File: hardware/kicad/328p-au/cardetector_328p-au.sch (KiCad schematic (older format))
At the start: 64 parts, among them IC1 ATMEGA328-A, K1 RELAY_1RT, P1 CONN_01X03, P2 ISP, P3 RELAY OUT, P4 TTL OUT, P5 I2C, Q1 BSS138, Q2 BC817-40, SW1 TACTILE_SW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

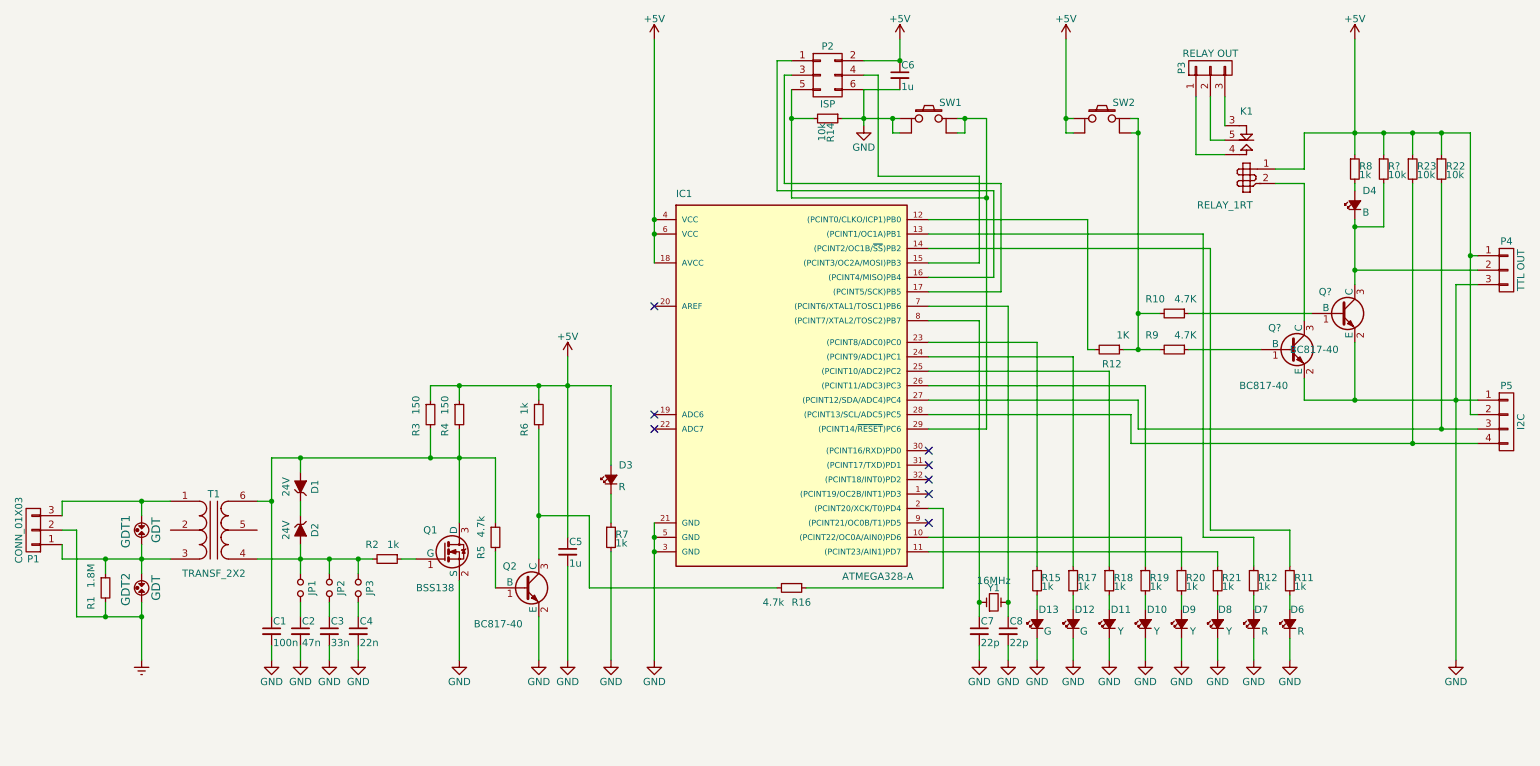
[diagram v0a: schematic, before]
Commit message: hardware/kicad/328p-au: separated output sheet
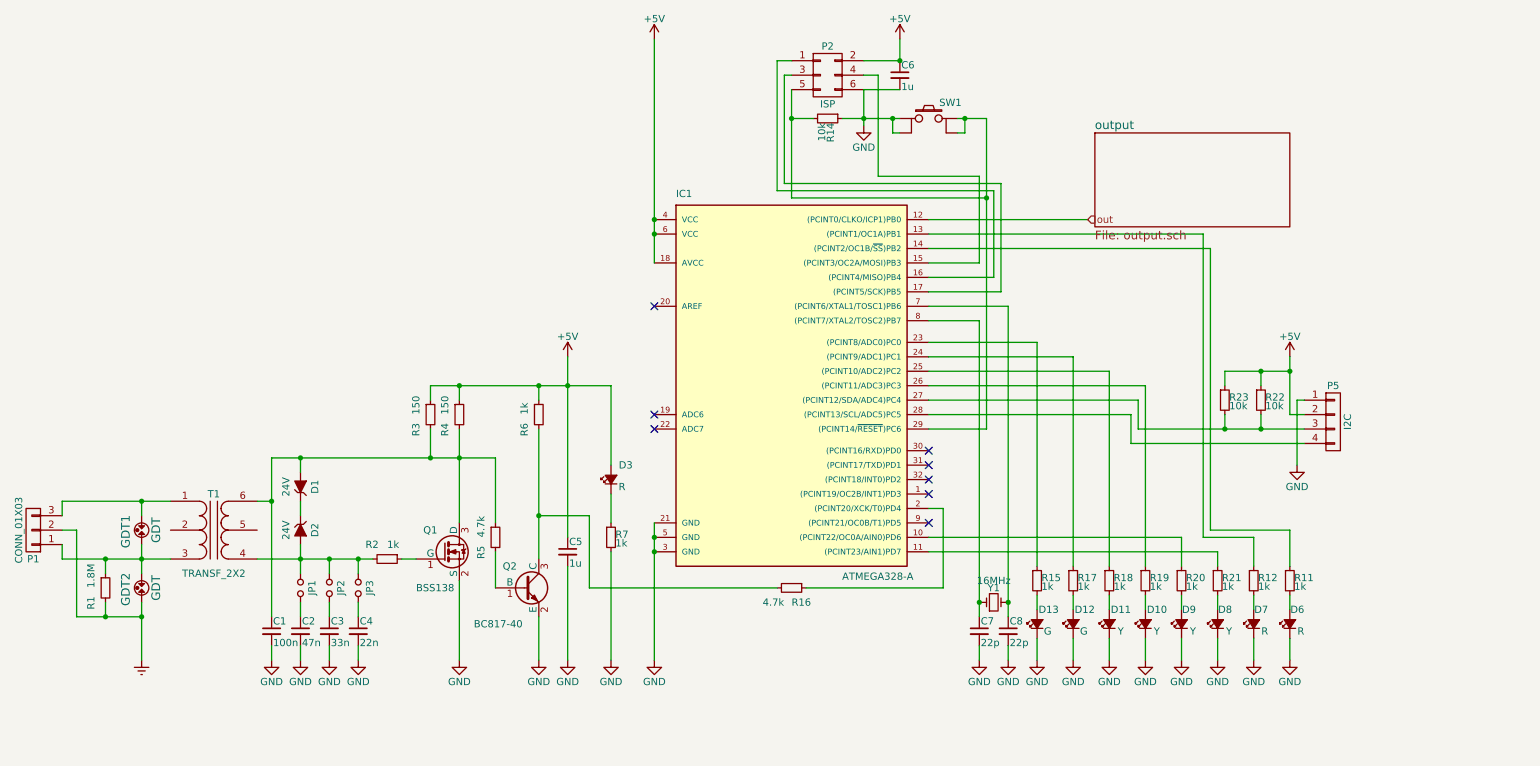
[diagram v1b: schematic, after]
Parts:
- removed D4: B, symbol Led_Small
- removed K1: RELAY_1RT, relays:SRD-SL-C, symbol RELAY_1RT
- removed P3: RELAY OUT, symbol CONN_01X03
- removed P4: TTL OUT, symbol CONN_01X03
- removed Q? (x2): BC817-40, SOT-23, symbol BC817-40
- removed R10, R9: 4.7K, symbol R_Small
- removed R12: 1K, symbol R_Small
- removed R8: 1k, symbol R_Small
- removed R?: 10k, symbol R_Small
- removed SW2: TACTILE_SW, symbol TACTILE_SW
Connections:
- net out: now reaches IC1.12 ((PCINT0/CLKO/ICP1)PB0)
- net at IC1.27 ((PCINT12/SDA/ADC4)PC4), P5.3 (P3), R22.2: now also R23.2
- net at IC1.28 ((PCINT13/SCL/ADC5)PC5), P5.4 (P4): no longer R23.2
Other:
- moved on the sheet: P5, R22, R23

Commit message: hardware/kicad/328p-au: separated collpits page, footprints assigned and imported to PCB
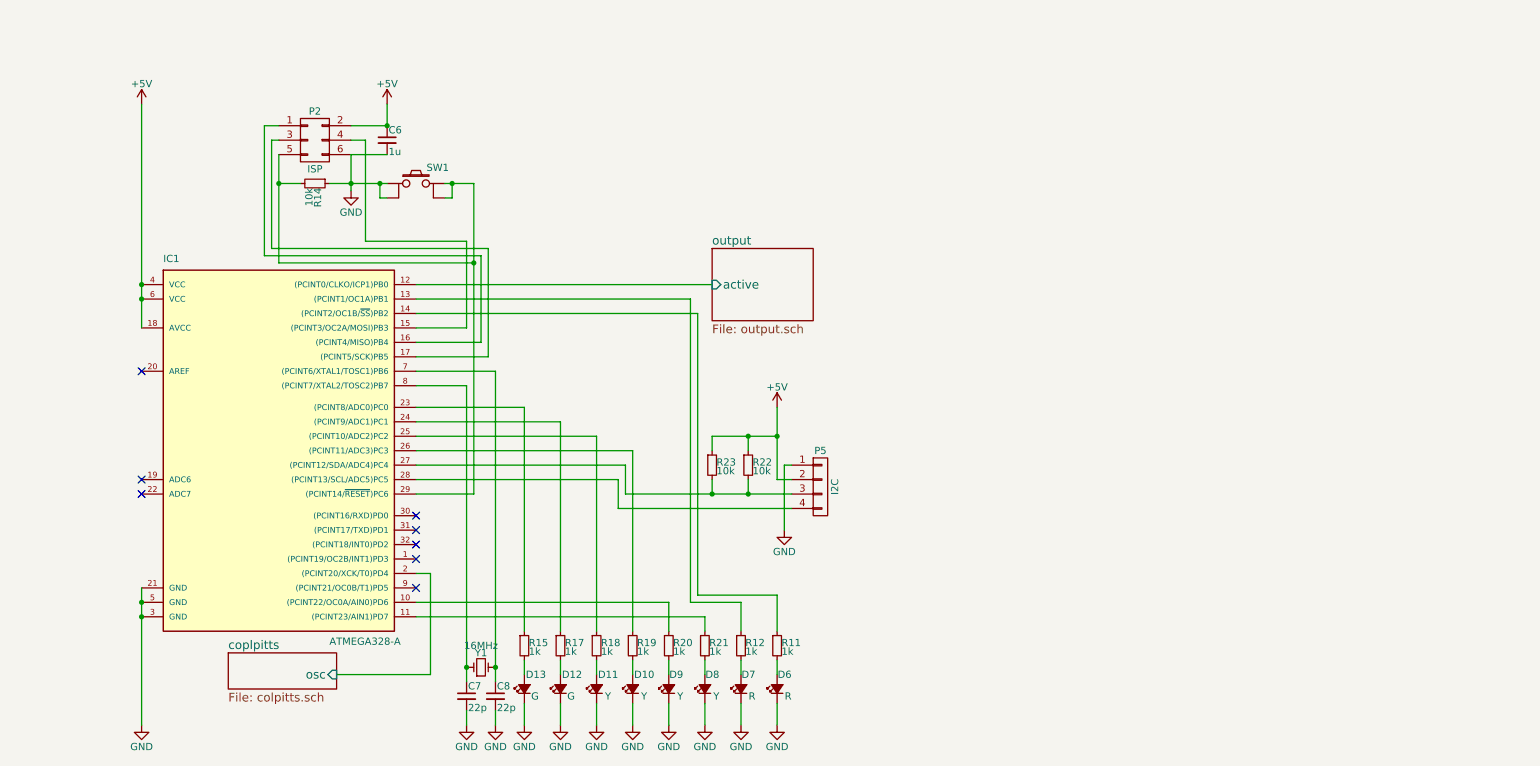
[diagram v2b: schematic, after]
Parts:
- removed C1: 100n, symbol C_Small
- removed C2: 47n, symbol C_Small
- removed C3: 33n, symbol C_Small
- removed C4: 22n, symbol C_Small
- removed C5: 1u, symbol C_Small
- removed D1, D2: 24V, symbol ZENERsmall
- removed D3: R, symbol Led_Small
- removed GDT1, GDT2: GDT, symbol GDT
- removed JP1, JP2, JP3: Jumper_NO_Small, symbol Jumper_NO_Small
- removed P1: CONN_01X03, symbol CONN_01X03
- removed Q1: BSS138, SOT-23, symbol BSS138
- removed Q2: BC817-40, SOT-23, symbol BC817-40
- removed R1: 1.8M, symbol R_Small
- removed R16, R5: 4.7k, symbol R_Small
- removed R2, R6, R7: 1k, symbol R_Small
- removed R3, R4: 150, symbol R_Small
- removed T1: TRANSF_2X2, symbol TRANSF_2X2
- C6, C7, C8: footprint (none) -> Capacitors_SMD:C_0603_HandSoldering
- D10, D11, D12, D13, D6, D7, D8, D9: footprint (none) -> gate433:SOD80C
- P2: footprint (none) -> Socket_Strips:Socket_Strip_Straight_2x03
- P5: footprint (none) -> Pin_Headers:Pin_Header_Straight_1x04
- R11, R12, R14, R15, R17, R18, R19, R20, R21, R22, R23: footprint (none) -> Resistors_SMD:R_0603_HandSoldering
- SW1: footprint (none) -> Buttons_Switches_ThroughHole:SW_TH_Tactile_Omron_B3F-10xx
- Y1: footprint (none) -> Crystals:Crystal_HC49-U_Vertical
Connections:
- net coplpitts/osc: now reaches IC1.2 ((PCINT20/XCK/T0)PD4)
- net out renamed output/active
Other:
- moved on the sheet: C6, C7, C8, D10, D11, D12, D13, D6, D7, D8, D9, IC1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

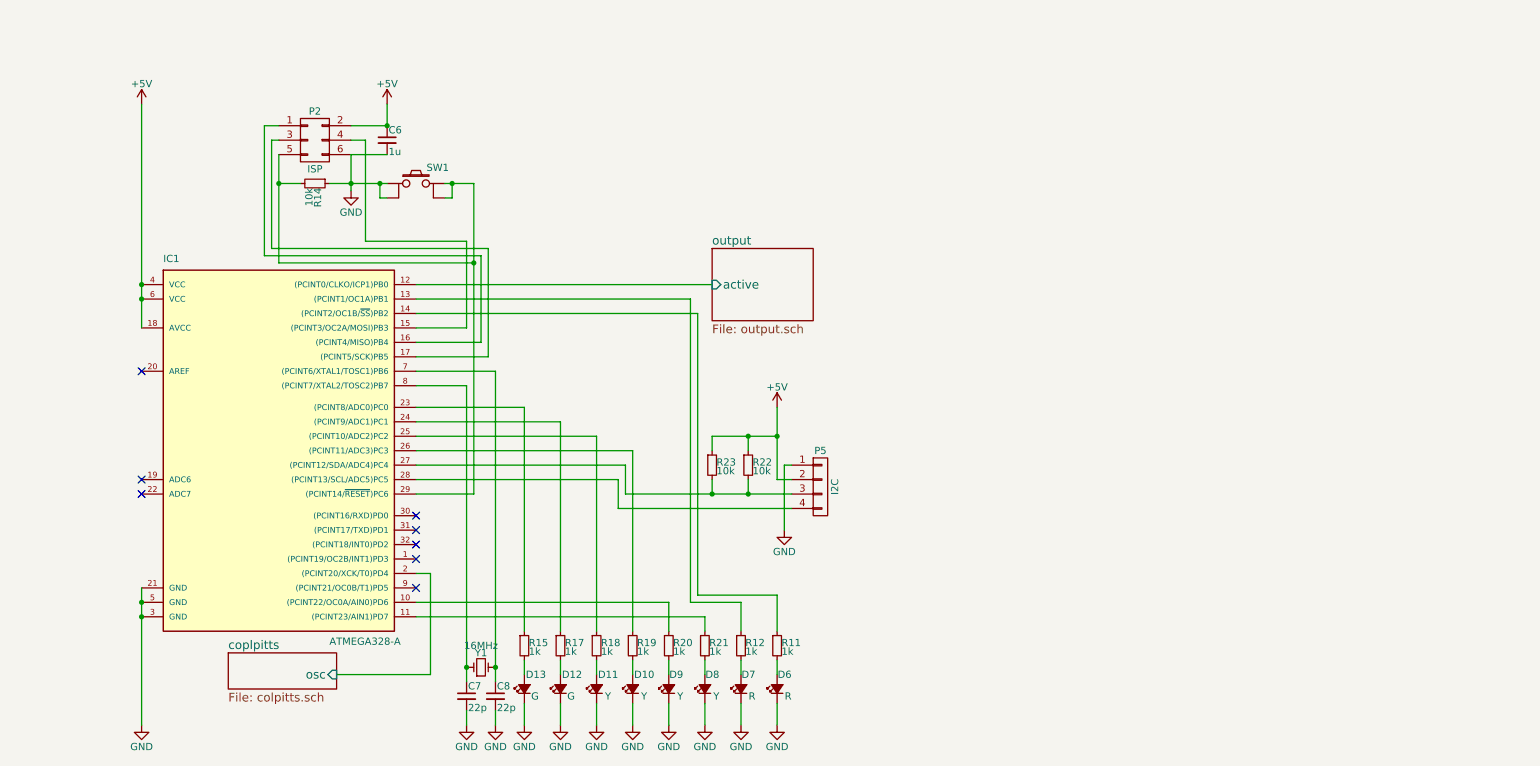
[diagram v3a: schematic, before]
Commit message: hardware/kicad: added serial connector && 3 push buttons
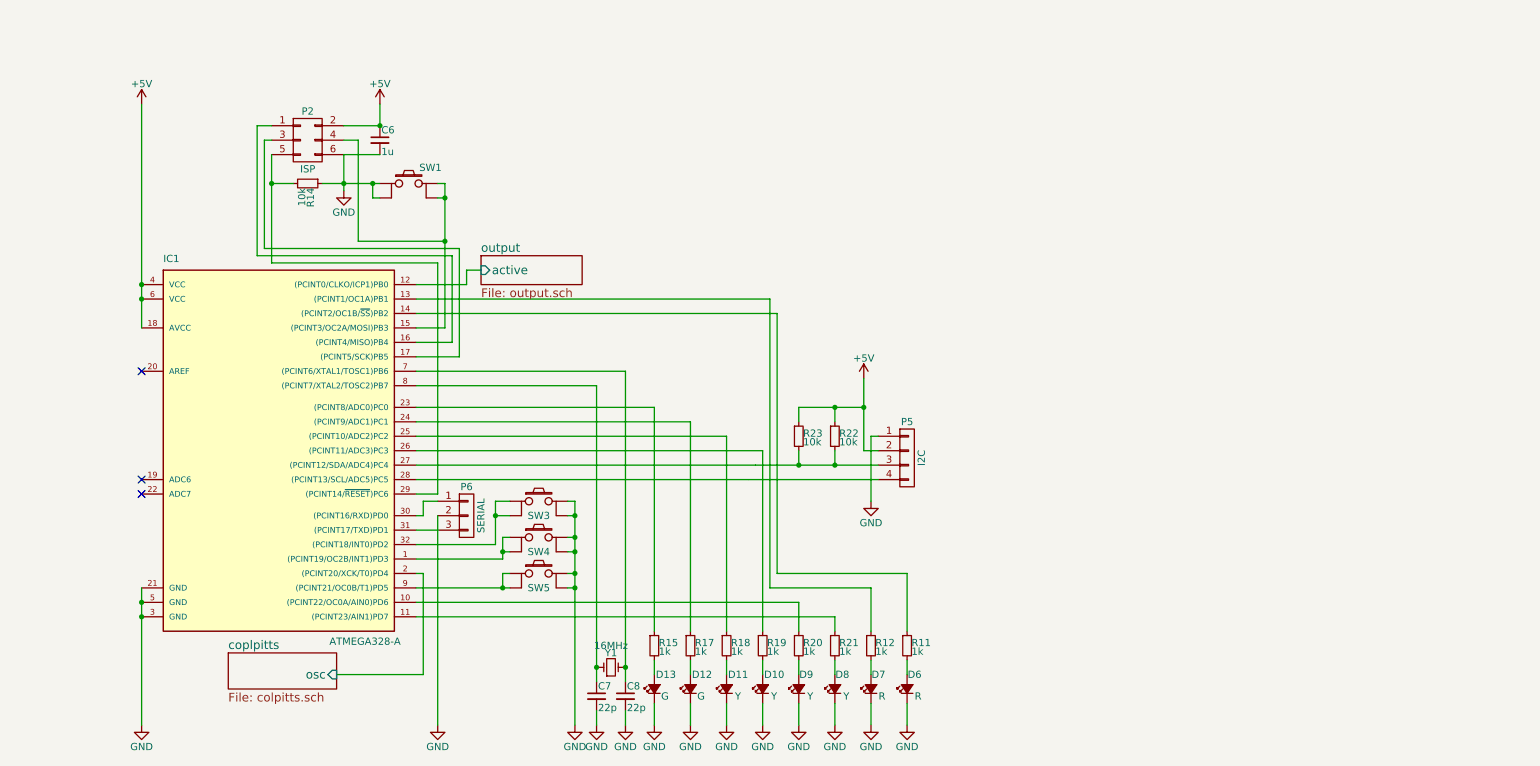
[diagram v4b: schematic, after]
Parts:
- added P6: SERIAL, Pin_Headers:Pin_Header_Straight_1x03, symbol CONN_01X03
- added SW3, SW4, SW5: TACTILE_SW, Buttons_Switches_ThroughHole:SW_TH_Tactile_Omron_B3F-10xx, symbol TACTILE_SW
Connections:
- net GND: now also P6.2 (P2), SW3.3, SW3.4, SW4.3, SW4.4, SW5.3, SW5.4
- net at IC1.15 ((PCINT3/OC2A/MOSI)PB3), P2.4 (P4): now also SW1.3, SW1.4
- net at IC1.29 ((PCINT14/~RESET~)PC6), P2.5 (P5), R14.2: no longer SW1.3, SW1.4
- net at IC1.1 ((PCINT19/OC2B/INT1)PD3): now also SW4.1, SW4.2
- net at IC1.30 ((PCINT16/RXD)PD0): now also P6.1 (P1)
- net at IC1.31 ((PCINT17/TXD)PD1): now also P6.3 (P3)
- net at IC1.32 ((PCINT18/INT0)PD2): now also SW3.1, SW3.2
- net at IC1.9 ((PCINT21/OC0B/T1)PD5): now also SW5.1, SW5.2
- no-connect marks 8 -> 3
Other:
- moved on the sheet: C6, C7, C8, D10, D11, D12, D13, D6, D7, D8, D9, P2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
